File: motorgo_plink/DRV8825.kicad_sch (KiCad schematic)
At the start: 13 parts, among them J8 Conn_01x02_Pin, U4 DRV8874PWPR

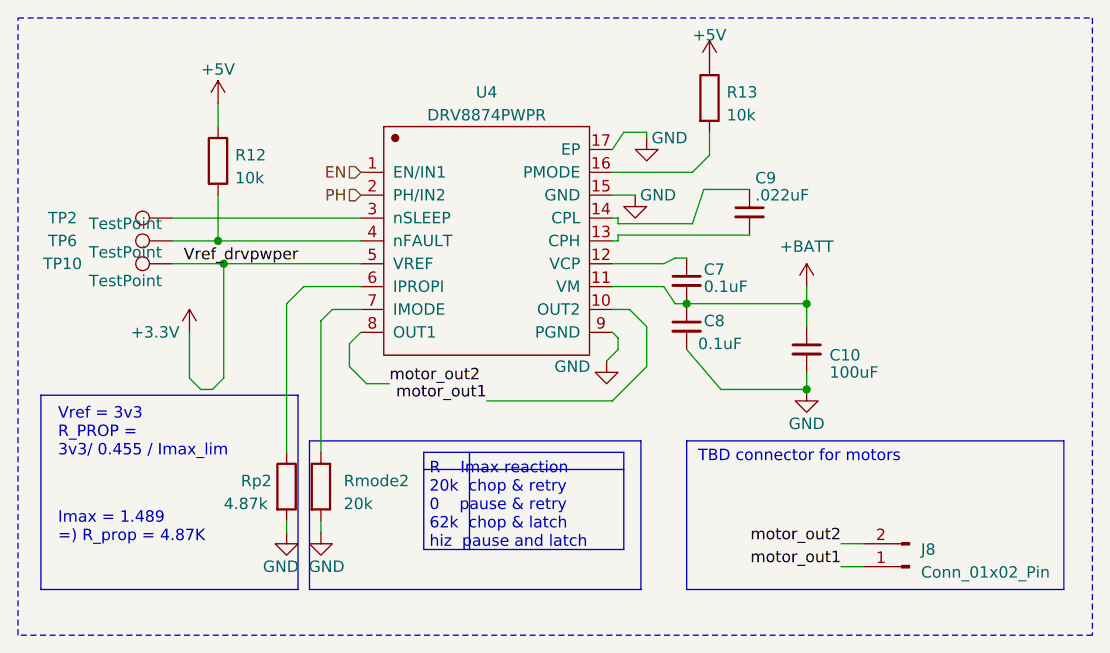
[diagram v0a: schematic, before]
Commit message: wip layout work begun, board dimensions finalized
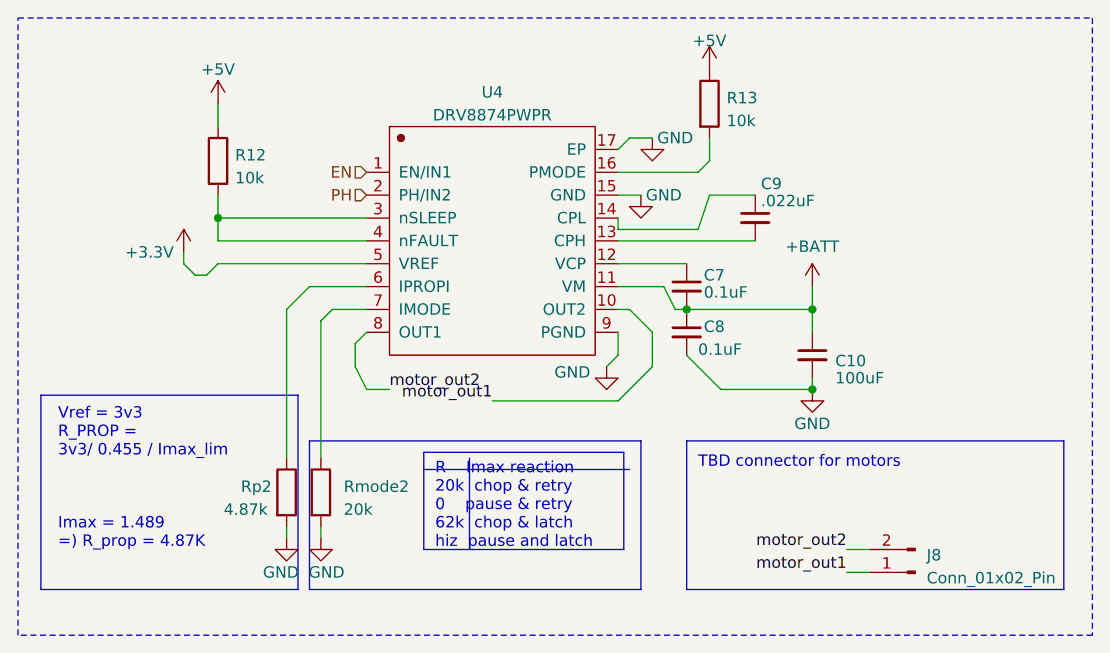
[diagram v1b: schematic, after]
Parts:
- removed TP10, TP2, TP6: TestPoint, TestPoint:TestPoint_Pad_1.0x1.0mm, symbol Connector:TestPoint
- J8: footprint Connector_PinHeader_2.54mm:PinHeader_1x02_P2.54mm_Vertical -> Connector_Molex:Molex_KK-254_AE-6410-02A_1x02_P2.54mm_Vertical
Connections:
- net at U4.3 (nSLEEP): now also R12.2, U4.4 (nFAULT)
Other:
- moved on the sheet: C10, C7, C8, C9, J8, R13, Rmode2, Rp2, U4

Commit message: production files and all edits for final send off of v1.0
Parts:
- J10: renamed from J8; LCSC_Part_Number C7430358 -> C722716
- R14: renamed from R12; LCSC_Part_Number C2906885 -> C25744
- R15: renamed from R13; LCSC_Part_Number C2906885 -> C25744
- renumbered C7 to C11, C8 to C12, C9 to C13, C10 to C14, Rmode2 to Rmode3, Rp2 to Rp3, U4 to U5

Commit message: update to recent production files
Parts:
- C11, C12: value 0.1uF -> 0.1uF 16v
- C14: value 100uF -> 100uF 25v
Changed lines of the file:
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@@
 			)
 		)
-		(property "Value" "0.1uF"
+		(property "Value" "0.1uF 16v"
 			(at 165.1 104.7813 0)
 			(effects
@@
 			)
 		)
-		(property "Value" "100uF"
+		(property "Value" "100uF 25v"
 			(at 180.34 107.9563 0)
 			(effects
@@
 			)
 		)
-		(property "Value" "0.1uF"
+		(property "Value" "0.1uF 16v"
 			(at 165.735 98.4313 0)
 			(effects
